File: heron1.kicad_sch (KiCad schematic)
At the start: 12 parts, among them J1 Conn_01x11_Pin, J2 Conn_01x11_Pin, J3 MotorA, J4 Motor B, SW1 SW_Push, U1 DRV8835

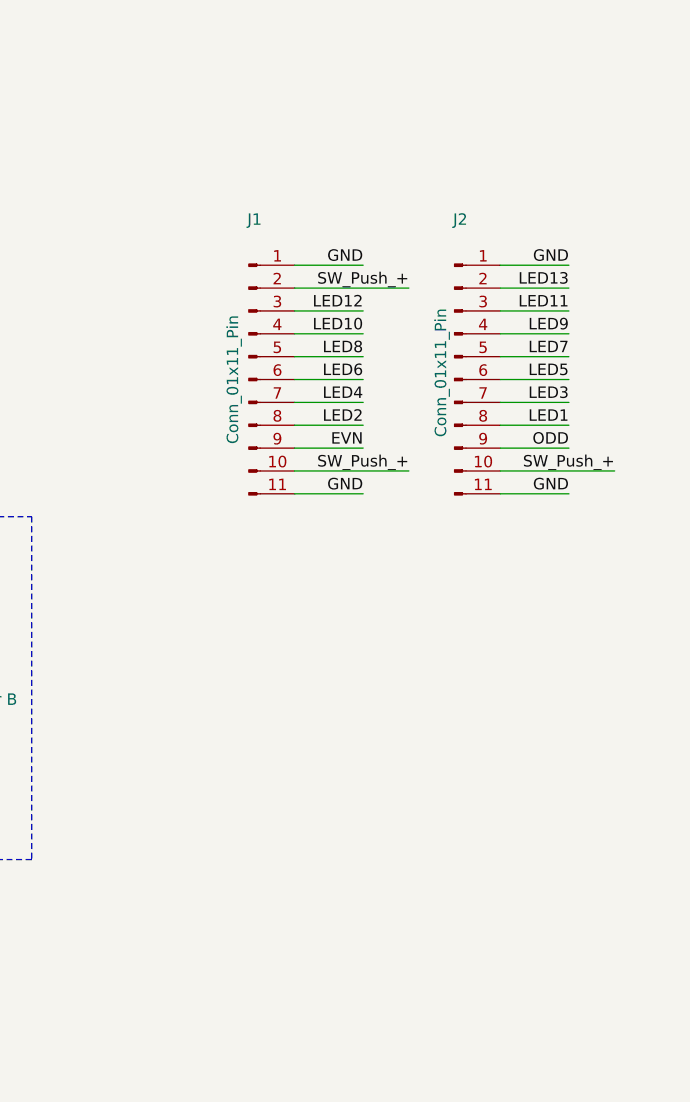
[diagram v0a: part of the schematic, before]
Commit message: added new drivers
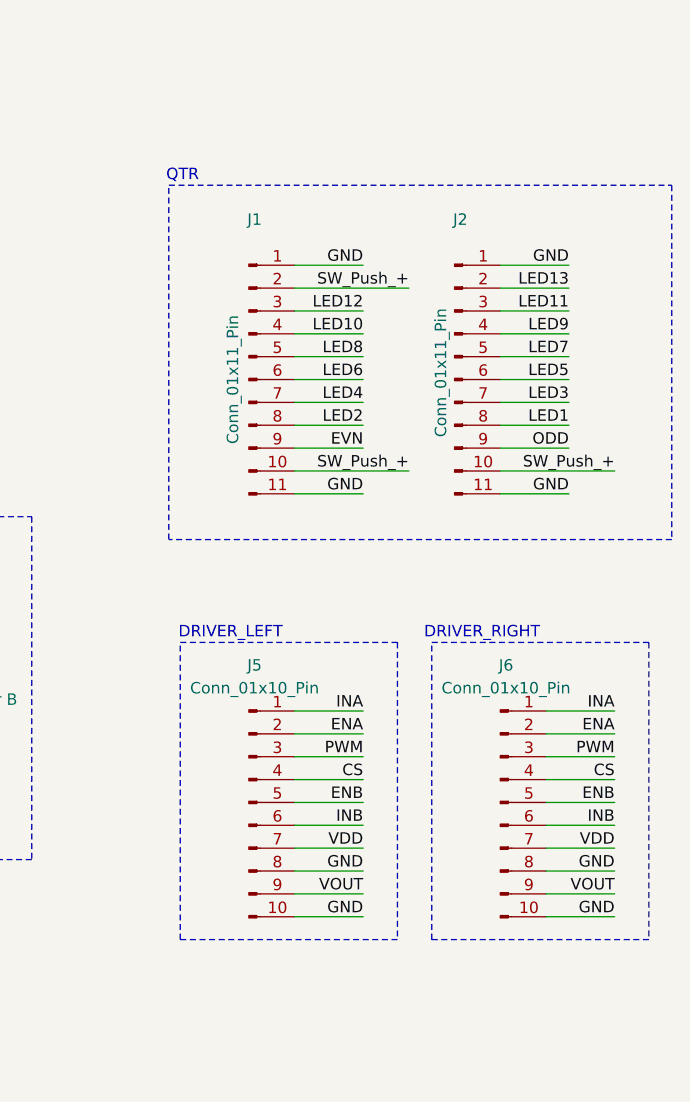
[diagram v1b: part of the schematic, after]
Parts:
- added J5, J6: Conn_01x10_Pin, symbol Connector:Conn_01x10_Pin
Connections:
- net GND: now also J5.10 (Pin_10), J5.8 (Pin_8), J6.10 (Pin_10), J6.8 (Pin_8)
- new net CS: J5.4 (Pin_4), J6.4 (Pin_4)
- new net ENA: J5.2 (Pin_2), J6.2 (Pin_2)
- new net ENB: J5.5 (Pin_5), J6.5 (Pin_5)
- new net INA: J5.1 (Pin_1), J6.1 (Pin_1)
- new net INB: J5.6 (Pin_6), J6.6 (Pin_6)
- new net PWM: J5.3 (Pin_3), J6.3 (Pin_3)
- new net VDD: J5.7 (Pin_7), J6.7 (Pin_7)
- new net VOUT: J5.9 (Pin_9), J6.9 (Pin_9)
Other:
- note added: "DRIVER_LEFT"
- note added: "DRIVER_RIGHT"
- note added: "QTR"

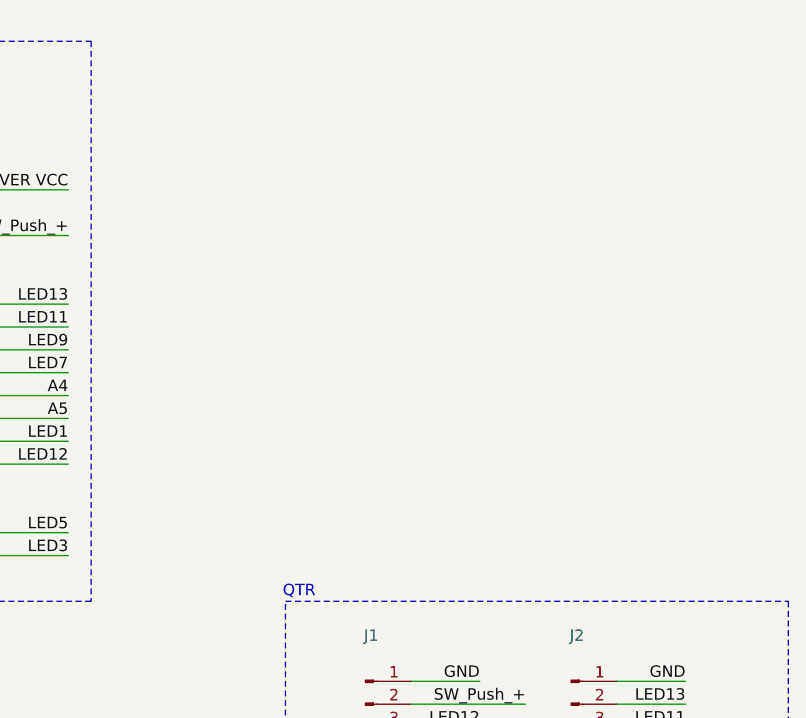
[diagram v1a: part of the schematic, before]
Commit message: added arduino nano 33 iot
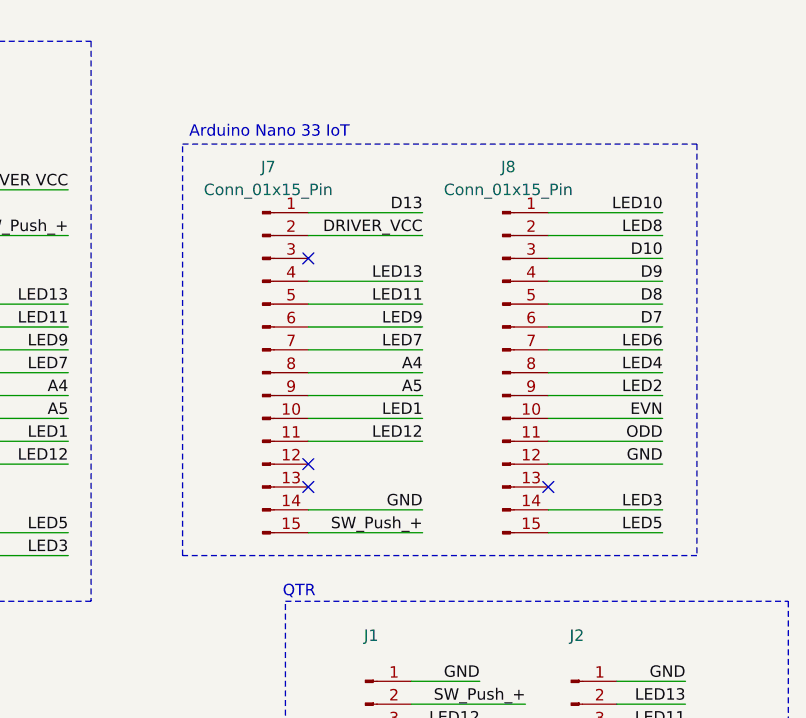
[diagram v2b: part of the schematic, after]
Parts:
- added J7, J8: Conn_01x15_Pin, symbol Connector:Conn_01x15_Pin
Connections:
- net A4: now also J7.8 (Pin_8)
- net A5: now also J7.9 (Pin_9)
- net D10: now also J8.3 (Pin_3)
- net D13: now also J7.1 (Pin_1)
- net D7: now also J8.6 (Pin_6)
- net D8: now also J8.5 (Pin_5)
- net D9: now also J8.4 (Pin_4)
- net EVN: now also J8.10 (Pin_10)
- net GND: now also J7.14 (Pin_14), J8.12 (Pin_12)
- net LED1: now also J7.10 (Pin_10)
- net LED10: now also J8.1 (Pin_1)
- net LED11: now also J7.5 (Pin_5)
- net LED12: now also J7.11 (Pin_11)
- net LED13: now also J7.4 (Pin_4)
- net LED2: now also J8.9 (Pin_9)
- net LED3: now also J8.14 (Pin_14)
- net LED4: now also J8.8 (Pin_8)
- net LED5: now also J8.15 (Pin_15)
- net LED6: now also J8.7 (Pin_7)
- net LED7: now also J7.7 (Pin_7)
- net LED8: now also J8.2 (Pin_2)
- net LED9: now also J7.6 (Pin_6)
- net ODD: now also J8.11 (Pin_11)
- net SW_Push_+: now also J7.15 (Pin_15)
- new net DRIVER_VCC: J7.2 (Pin_2)
- no-connect marks 4 -> 8

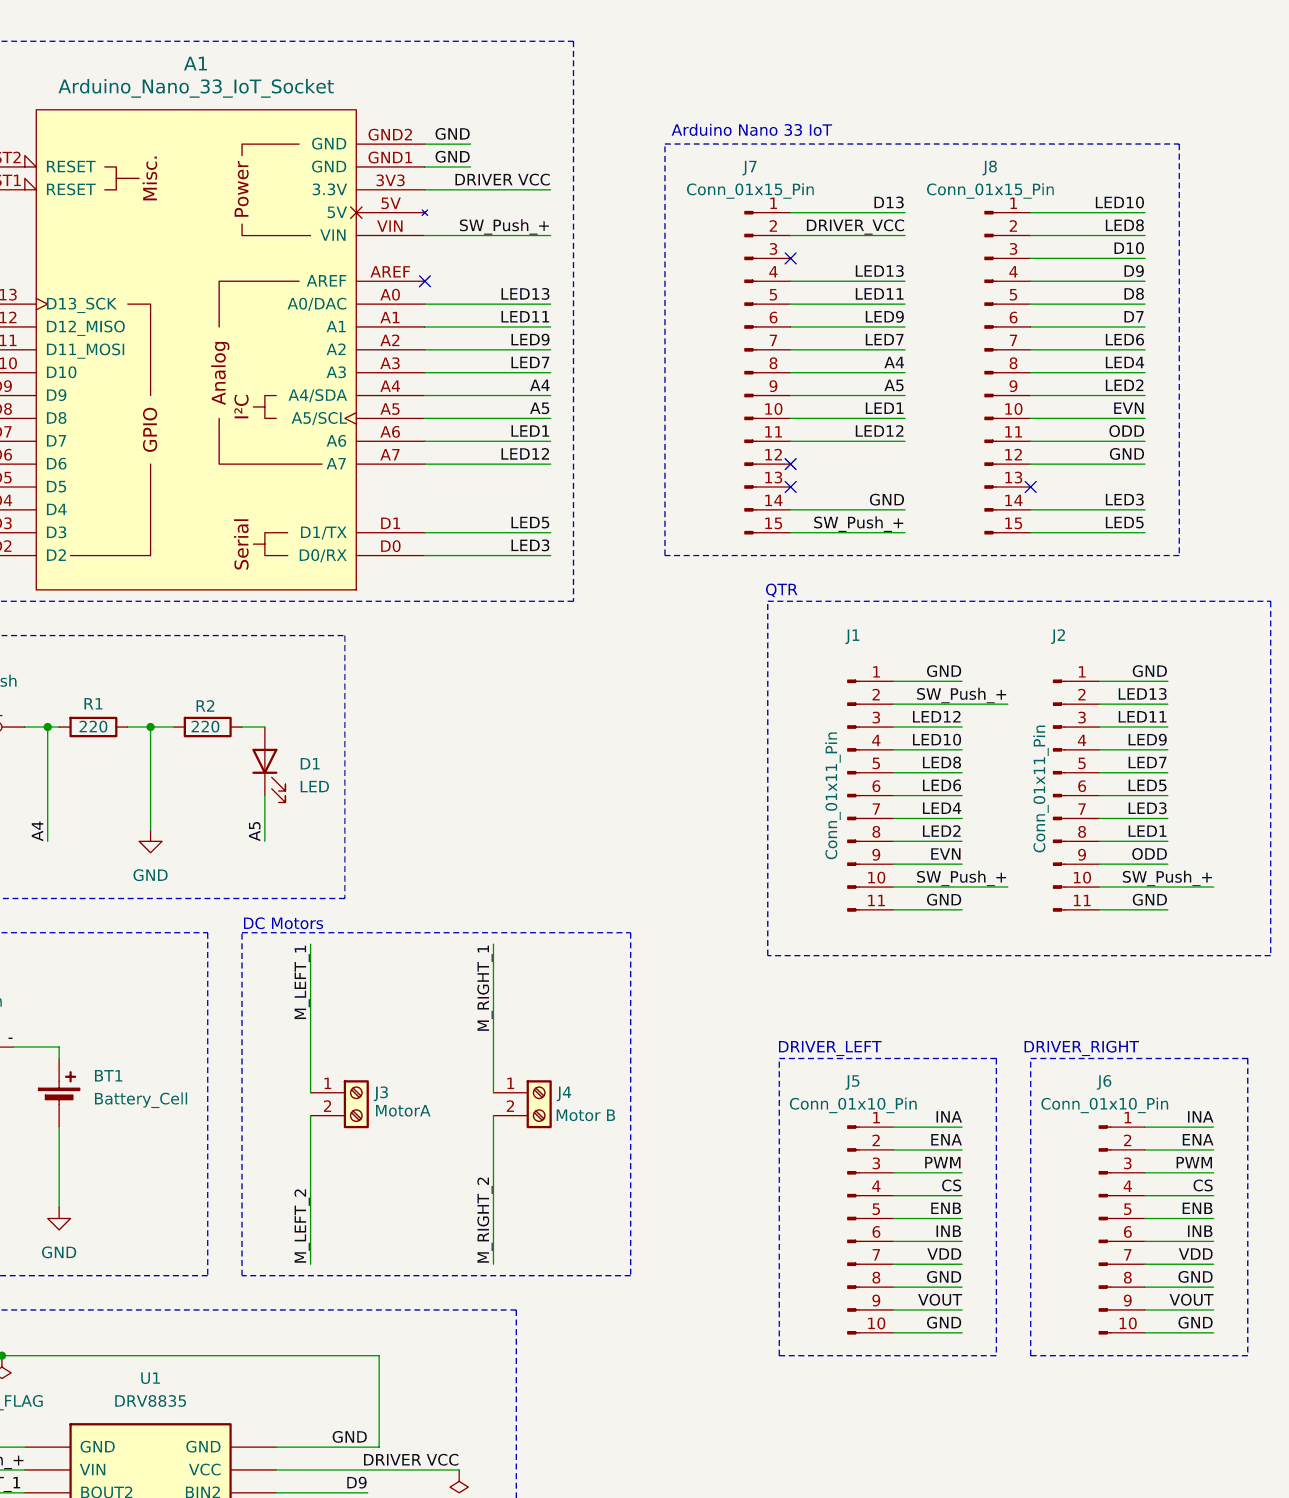
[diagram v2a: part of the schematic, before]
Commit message: started connecting new drivers
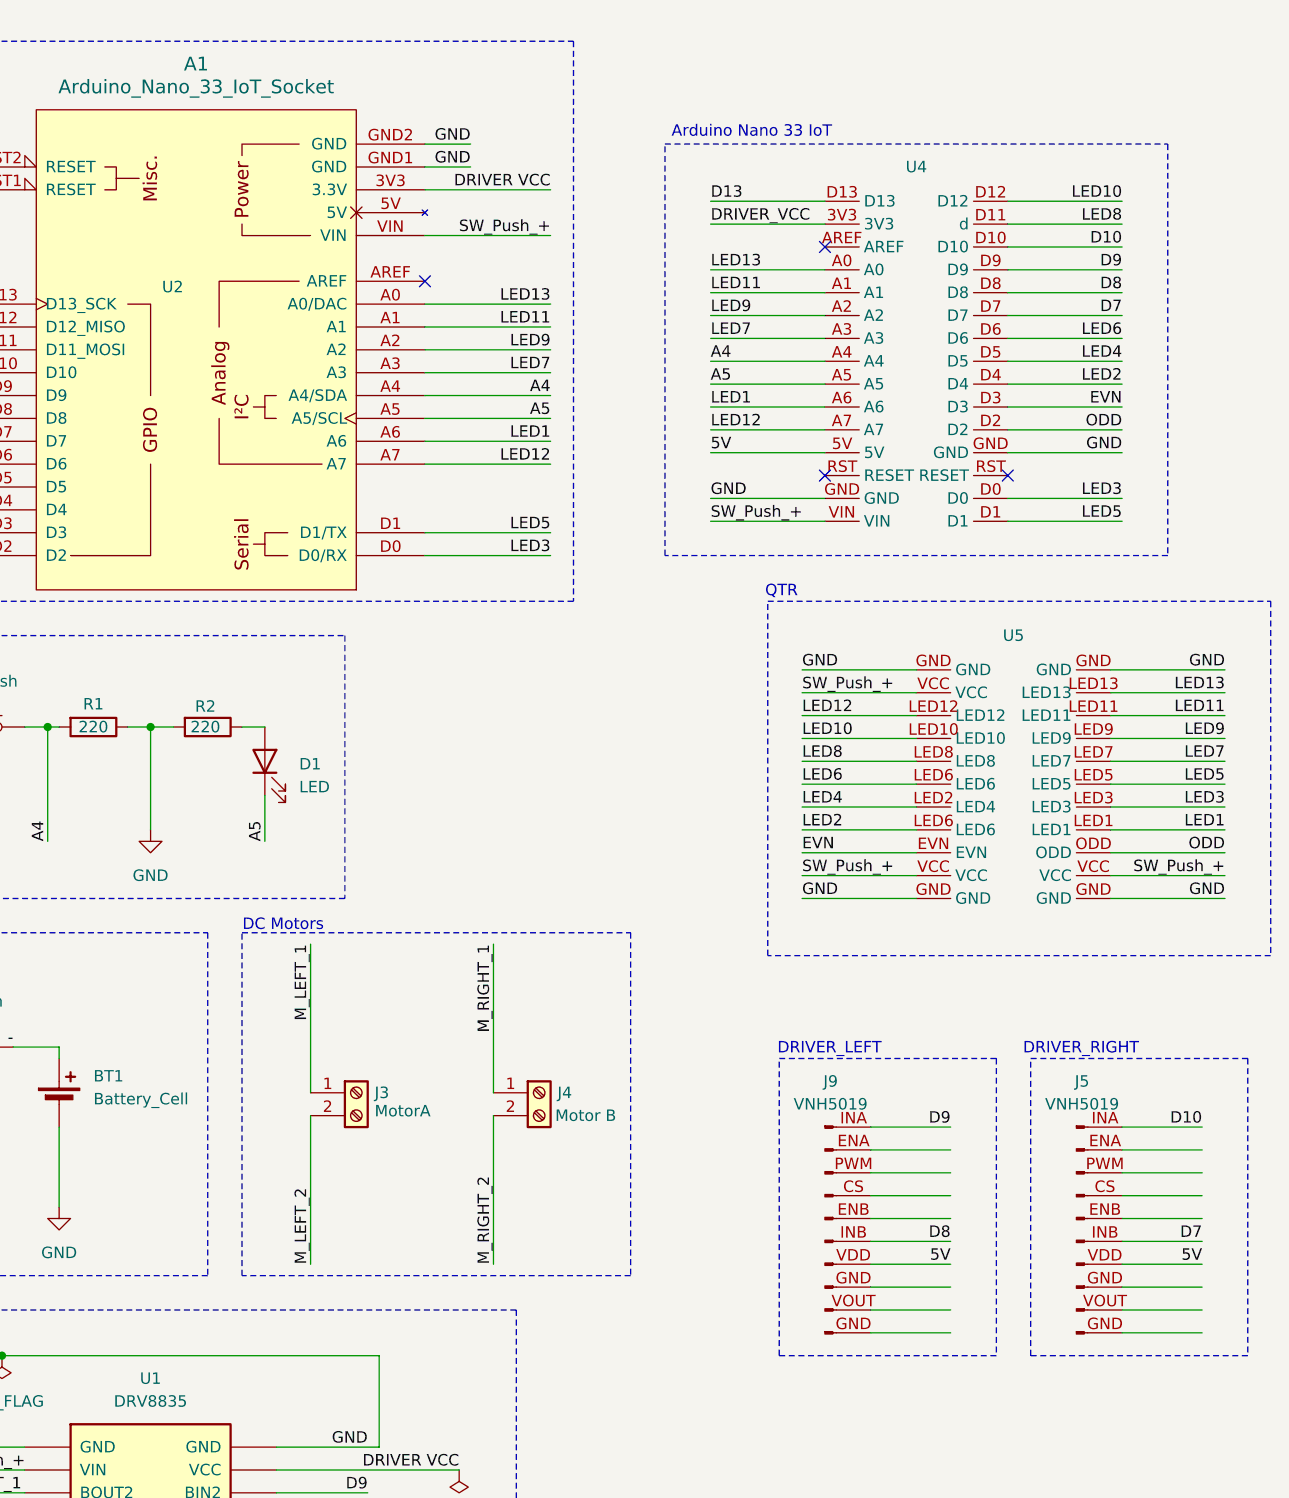
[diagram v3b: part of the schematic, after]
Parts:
- removed J1, J2: Conn_01x11_Pin, Connector_PinHeader_2.54mm:PinHeader_1x11_P2.54mm_Vertical, symbol Connector:Conn_01x11_Pin
- removed J5, J6: Conn_01x10_Pin, symbol Connector:Conn_01x10_Pin
- removed J7, J8: Conn_01x15_Pin, symbol Connector:Conn_01x15_Pin
- added J5, J9: VNH5019, symbol heron_symbols:VNH5019
- added U2: ~, symbol heron_symbols:Arduino_Nano_33_Iot
- added U3, U4: ~, symbol heron_symbols:Arduino_Nano_33_IoT
- added U5: ~, symbol heron_symbols:QTR_13
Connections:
- net A4: now also U4.A4
- net A5: now also U4.A5
- net D10: now also J5.INA, U4.D10
- net D13: now also U4.D13
- net D7: now also J5.INB, U4.D7
- net D8: now also J9.INB, U4.D8
- net D9: now also J9.INA, U4.D9
- net DRIVER_VCC: now also U4.3V3
- net EVN: now also U4.D3, U5.EVN
- net GND: now also U4.GND, U5.GND
- net LED1: now also U4.A6, U5.LED1
- net LED10: now also U4.D12, U5.LED10
- net LED11: now also U4.A1, U5.LED11
- net LED12: now also U4.A7, U5.LED12
- net LED13: now also U4.A0, U5.LED13
- net LED2: now also U4.D4, U5.LED6
- net LED3: now also U4.D0, U5.LED3
- net LED4: now also U4.D5, U5.LED2 (LED4)
- net LED5: now also U4.D1, U5.LED5
- net LED6: now also U4.D6, U5.LED6
- net LED7: now also U4.A3, U5.LED7
- net LED8: now also U4.D11 (d), U5.LED8
- net LED9: now also U4.A2, U5.LED9
- net ODD: now also U4.D2, U5.ODD
- net SW_Push_+: now also U4.VIN, U5.VCC
- new net 5V: J5.VDD, J9.VDD, U4.5V
- no-connect marks 8 -> 7
